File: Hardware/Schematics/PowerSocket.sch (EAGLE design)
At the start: 28 parts, among them IC1 REG1117, U1 ESP-32S

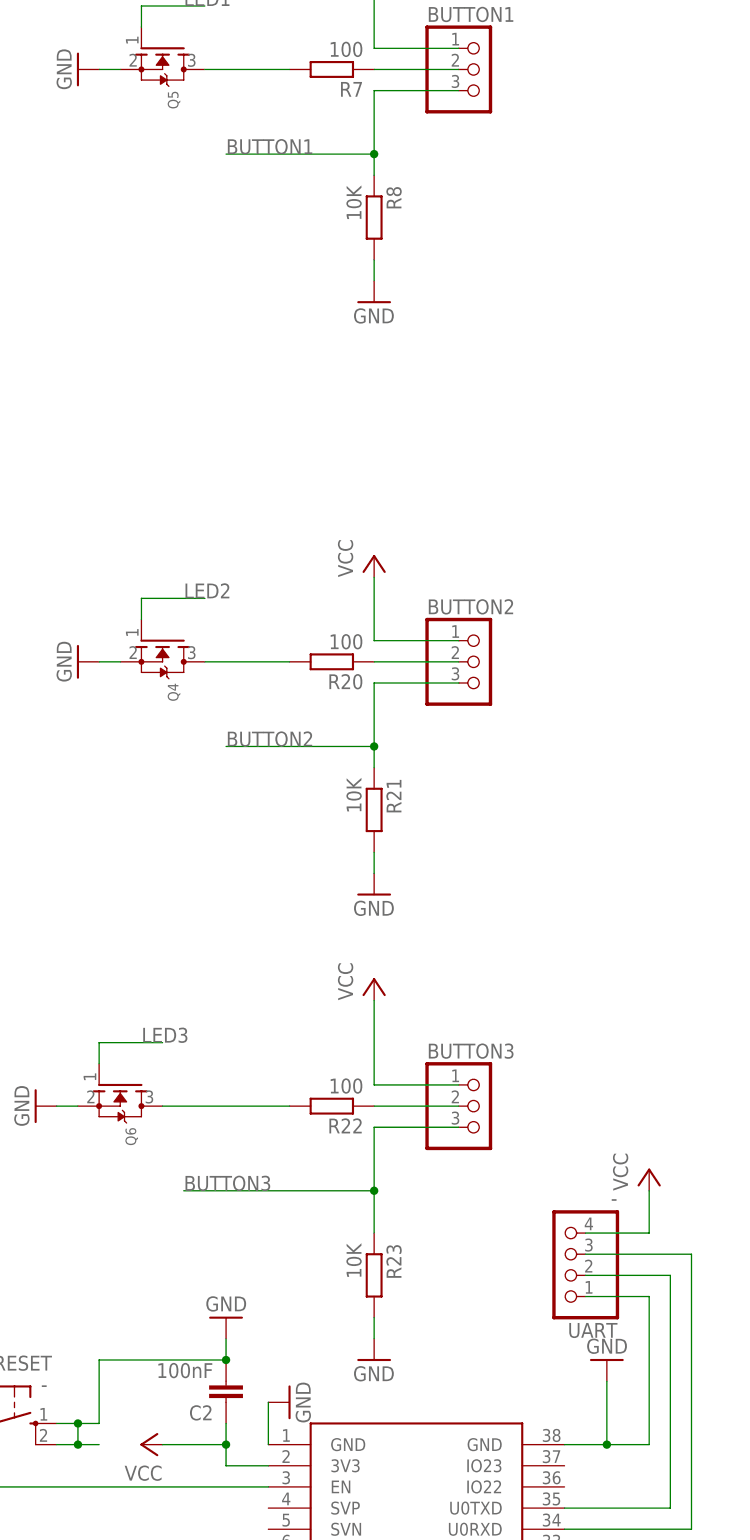
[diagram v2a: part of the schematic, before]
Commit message: Removed some pullups, as the ESP support this in hardware.
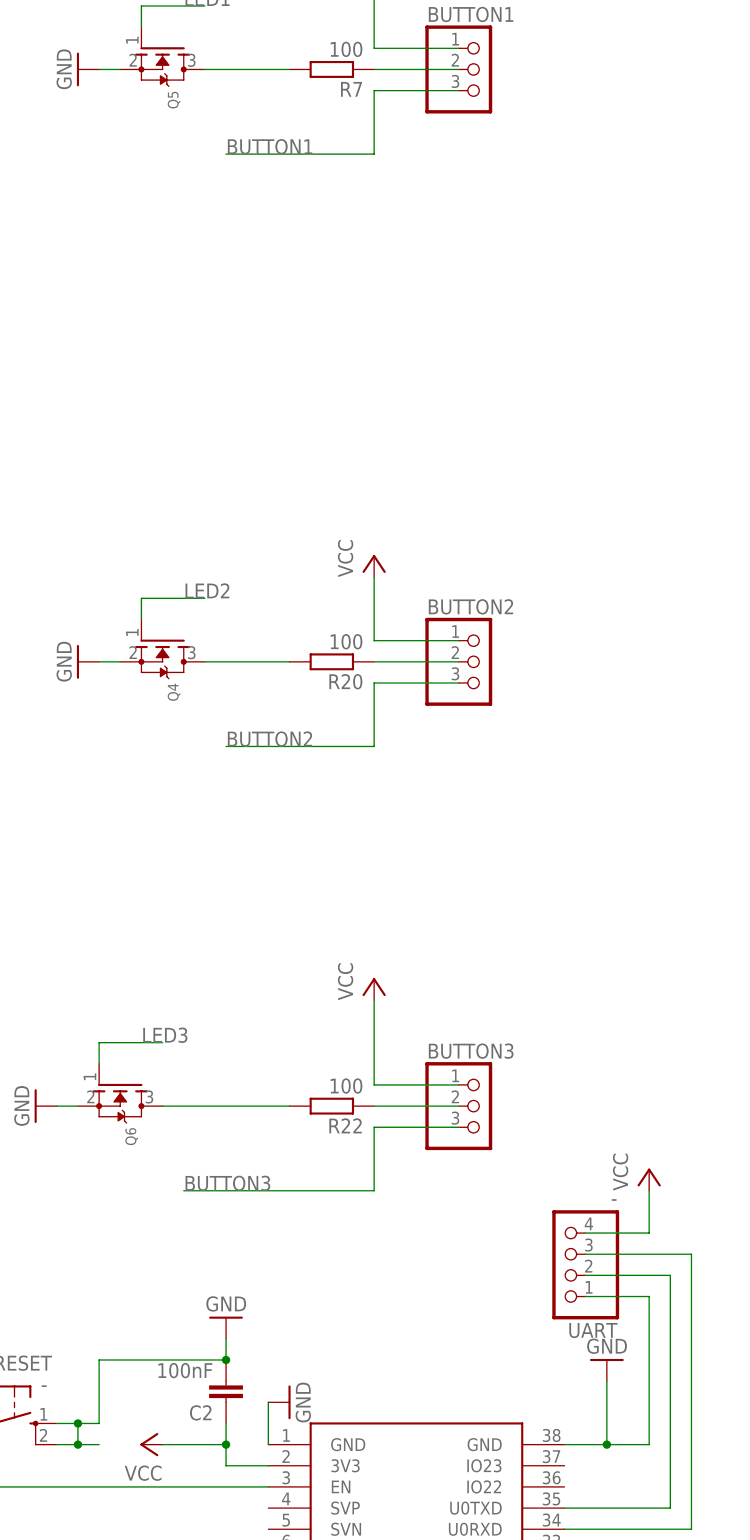
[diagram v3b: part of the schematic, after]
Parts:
- removed R21, R23, R8: 10K, rcl:R-EU_R0805
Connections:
- net BUTTON1: no longer R8.1
- net BUTTON2: no longer R21.1
- net BUTTON3: no longer R23.1
- net GND: no longer R21.2, R23.2, R8.2
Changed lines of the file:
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@@
 <setting verticaltext="up"/>
 </settings>
-<grid distance="0.5" unitdist="mm" unit="mm" style="lines" multiple="1" display="no" altdistance="0.01" altunitdist="inch" altunit="inch"/>
+<grid distance="0.1" unitdist="inch" unit="inch" style="lines" multiple="1" display="no" altdistance="0.01" altunitdist="inch" altunit="inch"/>
 <layers>
 <layer number="1" name="Top" color="4" fill="1" visible="no" active="no"/>
@@
 <part name="R7" library="rcl" deviceset="R-EU_" device="R0805" value="100"/>
 <part name="P+8" library="supply1" deviceset="VCC" device=""/>
-<part name="R8" library="rcl" deviceset="R-EU_" device="R0805" value="10K"/>
-<part name="GND15" library="supply1" deviceset="GND" device=""/>
 <part name="GND" library="wirepad" deviceset="2,15/1,0" device="" value="GND"/>
 <part name="R20" library="rcl" deviceset="R-EU_" device="R0805" value="100"/>
 <part name="P+17" library="supply1" deviceset="VCC" device=""/>
-<part name="R21" library="rcl" deviceset="R-EU_" device="R0805" value="10K"/>
-<part name="GND18" library="supply1" deviceset="GND" device=""/>
 <part name="R22" library="rcl" deviceset="R-EU_" device="R0805" value="100"/>
 <part name="P+19" library="supply1" deviceset="VCC" device=""/>
-<part name="R23" library="rcl" deviceset="R-EU_" device="R0805" value="10K"/>
-<part name="GND19" library="supply1" deviceset="GND" device=""/>
 <part name="JTAG" library="pinhead" deviceset="PINHD-1X4" device="" value="-"/>
 <part name="BUTTON1" library="pinhead" deviceset="PINHD-1X3" device=""/>
@@
 <instance part="R7" gate="G$1" x="3" y="193.26" rot="R180"/>
 <instance part="P+8" gate="VCC" x="8.08" y="205.96"/>
-<instance part="R8" gate="G$1" x="8.08" y="175.48" rot="R270"/>
-<instance part="GND15" gate="1" x="8.08" y="165.32"/>
 <instance part="GND" gate="1" x="-73.5" y="-81" rot="R270"/>
 <instance part="R20" gate="G$1" x="3" y="122.14" rot="R180"/>
 <instance part="P+17" gate="VCC" x="8.08" y="134.84"/>
-<instance part="R21" gate="G$1" x="8.08" y="104.36" rot="R270"/>
-<instance part="GND18" gate="1" x="8.08" y="94.2"/>
 <instance part="R22" gate="G$1" x="3" y="68.8" rot="R180"/>
 <instance part="P+19" gate="VCC" x="8.08" y="84.04"/>
-<instance part="R23" gate="G$1" x="8.08" y="48.48" rot="R270"/>
-<instance part="GND19" gate="1" x="8.08" y="38.32"/>
 <instance part="JTAG" gate="A" x="5.54" y="-50.58" rot="R270"/>
 <instance part="BUTTON1" gate="A" x="20.78" y="193.26"/>
@@
 </segment>
 <segment>
-<pinref part="GND15" gate="1" pin="GND"/>
-<pinref part="R8" gate="G$1" pin="2"/>
-<wire x1="8.08" y1="167.86" x2="8.08" y2="170.4" width="0.1524" layer="91"/>
-</segment>
-<segment>
-<pinref part="R21" gate="G$1" pin="2"/>
-<pinref part="GND18" gate="1" pin="GND"/>
-<wire x1="8.08" y1="99.28" x2="8.08" y2="96.74" width="0.1524" layer="91"/>
-</segment>
-<segment>
-<pinref part="GND19" gate="1" pin="GND"/>
-<pinref part="R23" gate="G$1" pin="2"/>
-<wire x1="8.08" y1="40.86" x2="8.08" y2="43.4" width="0.1524" layer="91"/>
-</segment>
-<segment>
 <pinref part="FLASH" gate="1" pin="S1"/>
 <wire x1="0.46" y1="-98.84" x2="0.46" y2="-101.38" width="0.1524" layer="91"/>
@@
 </segment>
 <segment>
-<pinref part="R8" gate="G$1" pin="1"/>
-<wire x1="8.08" y1="180.56" x2="8.08" y2="183.1" width="0.1524" layer="91"/>
 <wire x1="8.08" y1="183.1" x2="-9.7" y2="183.1" width="0.1524" layer="91"/>
-<junction x="8.08" y="183.1"/>
 <label x="-9.7" y="183.1" size="1.778" layer="95"/>
 <pinref part="BUTTON1" gate="A" pin="3"/>
@@
 </segment>
 <segment>
-<pinref part="R21" gate="G$1" pin="1"/>
 <wire x1="8.08" y1="111.98" x2="-9.7" y2="111.98" width="0.1524" layer="91"/>
 <label x="-9.7" y="111.98" size="1.778" layer="95"/>
-<wire x1="8.08" y1="111.98" x2="8.08" y2="109.44" width="0.1524" layer="91"/>
 <pinref part="BUTTON2" gate="A" pin="3"/>
 <wire x1="18.24" y1="119.6" x2="8.08" y2="119.6" width="0.1524" layer="91"/>
 <wire x1="8.08" y1="111.98" x2="8.08" y2="119.6" width="0.1524" layer="91"/>
-<junction x="8.08" y="111.98"/>
 </segment>
 </net>
@@
 </segment>
 <segment>
-<pinref part="R23" gate="G$1" pin="1"/>
-<wire x1="8.08" y1="58.64" x2="8.08" y2="53.56" width="0.1524" layer="91"/>
 <wire x1="8.08" y1="58.64" x2="-14.78" y2="58.64" width="0.1524" layer="91"/>
 <label x="-14.78" y="58.64" size="1.778" layer="95"/>
@@
 <wire x1="18.24" y1="66.26" x2="8.08" y2="66.26" width="0.1524" layer="91"/>
 <wire x1="8.08" y1="66.26" x2="8.08" y2="58.64" width="0.1524" layer="91"/>
-<junction x="8.08" y="58.64"/>
-</segment>
-</net>
+</segment>
+</net>

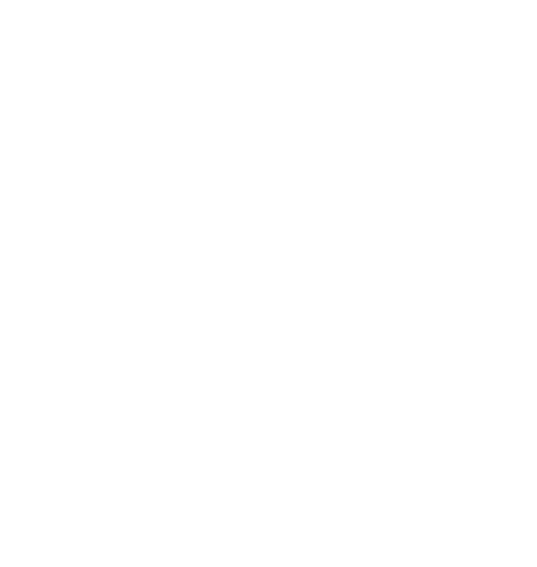
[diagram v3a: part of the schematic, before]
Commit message: Started implementing handling of button event. Code is not yet tested.
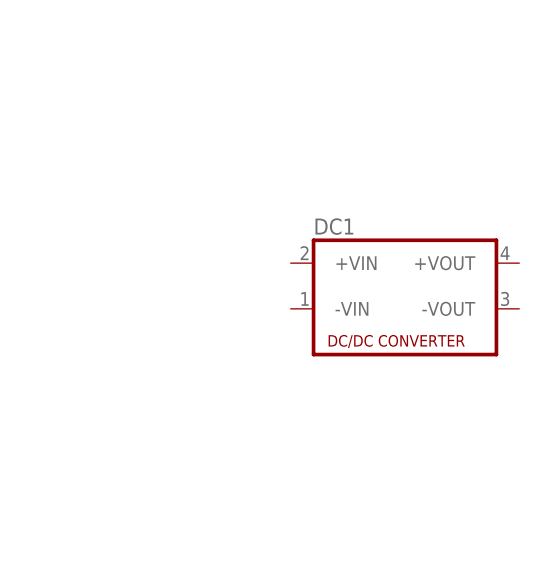
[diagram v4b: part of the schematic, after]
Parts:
- added DC1: (no value), dc-dc-converter:NME
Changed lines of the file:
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@@
 <?xml version="1.0" encoding="utf-8"?>
 <!DOCTYPE eagle SYSTEM "eagle.dtd">
-<eagle version="7.7.0">
+<eagle version="8.1.0">
 <drawing>
 <settings>
@@
 <part name="SUPPLY2" library="supply2" deviceset="+5V" device=""/>
 <part name="P+1" library="supply1" deviceset="VCC" device=""/>
+<part name="DC1" library="dc-dc-converter" deviceset="NME" device=""/>
 </parts>
 <sheets>
@@
 <instance part="SUPPLY2" gate="+5V" x="-65" y="-88" rot="R180"/>
 <instance part="P+1" gate="VCC" x="-105.5" y="-69.5" rot="R270"/>
+<instance part="DC1" gate="G$1" x="78.74" y="-76.2"/>
 </instances>
 <busses>
